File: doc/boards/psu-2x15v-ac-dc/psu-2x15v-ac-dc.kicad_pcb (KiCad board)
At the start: 2 copper layers, 60 x 52 mm, 28 parts, among them IC1 LM7815CT, IC2 LM7915CT, J7 Screw_Terminal_1x02, J9 Screw_Terminal_1x02, P1 CONN_01X03, P20 CONN_02X02

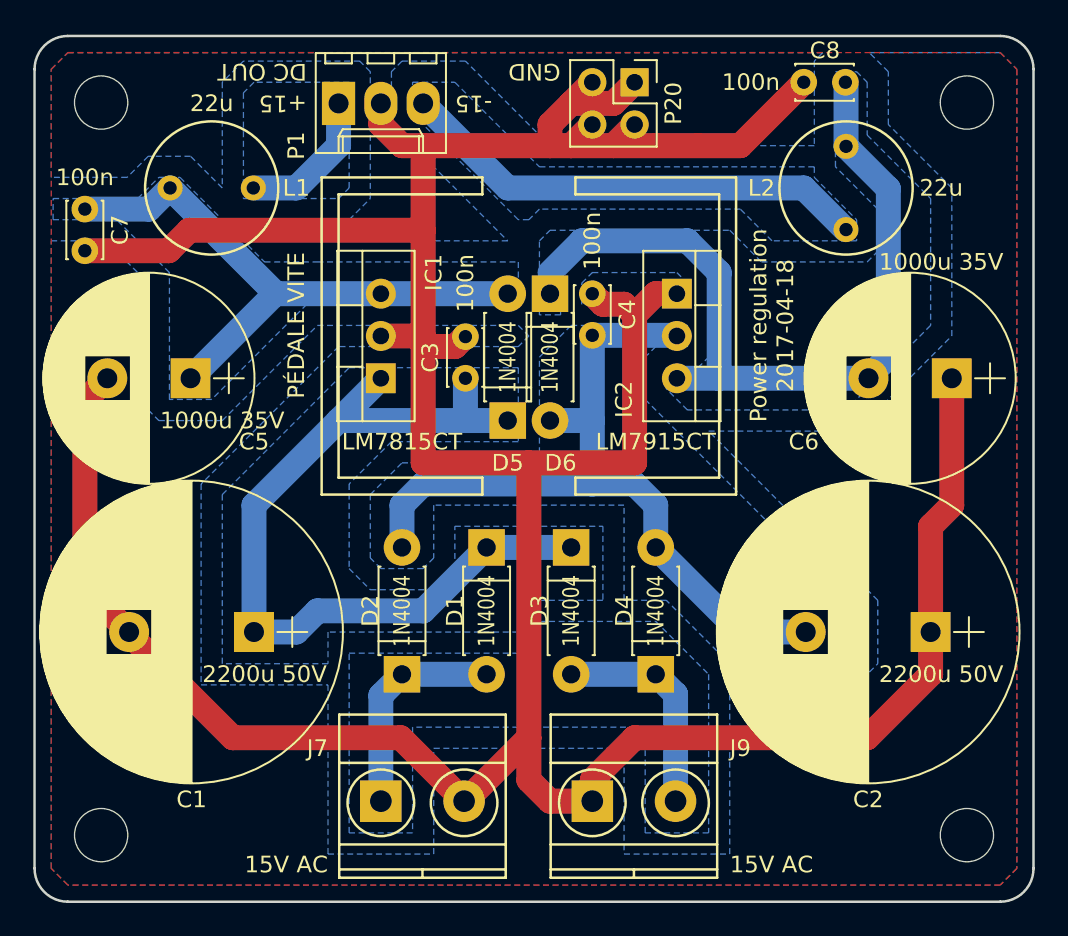
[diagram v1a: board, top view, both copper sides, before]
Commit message: Updated board files to KiCAD 6
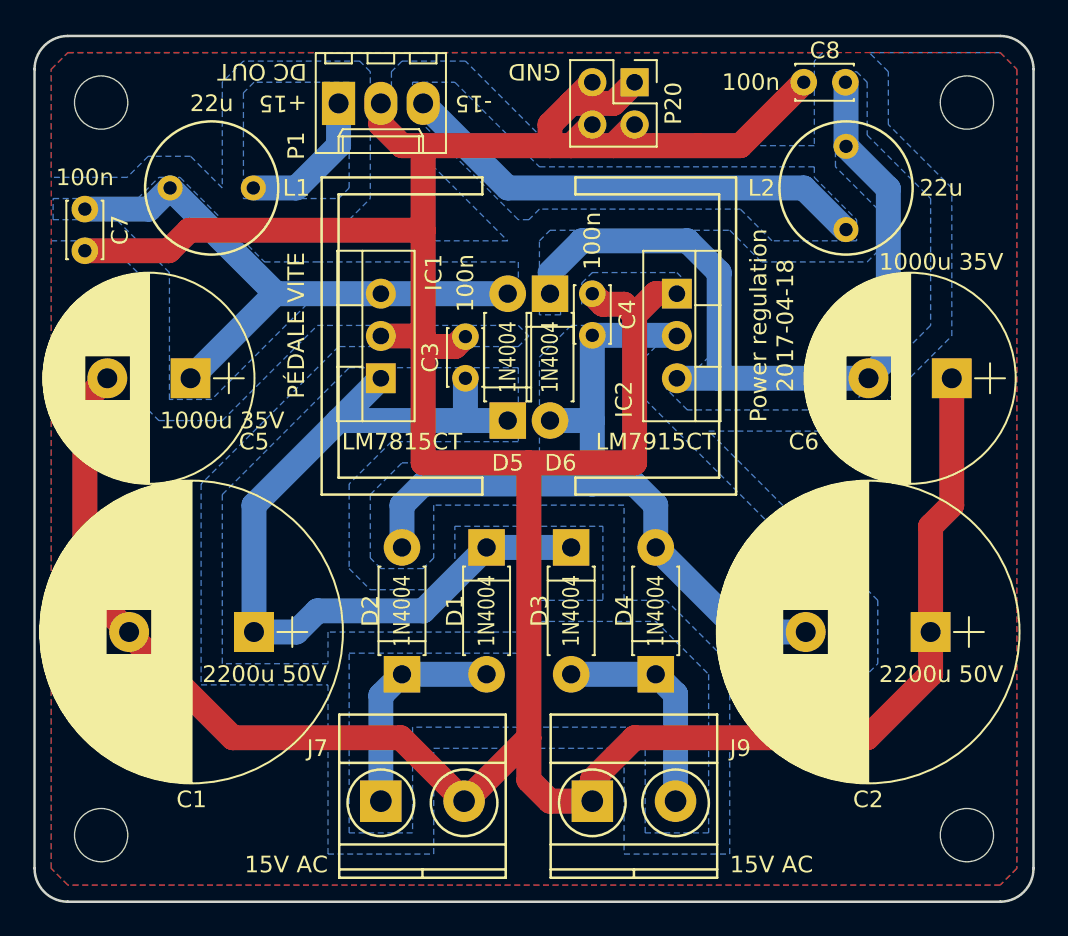
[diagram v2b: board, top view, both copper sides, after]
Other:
- net class Default removed
- net class Larger removed
- net class Power removed
- net class Power2 removed
- net class Power3 removed
